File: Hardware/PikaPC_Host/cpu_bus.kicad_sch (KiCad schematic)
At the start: 33 parts, among them SW1 SW_Push, U1 PPC403GA, U3 MCP120-315GI/TO, Y1 25M

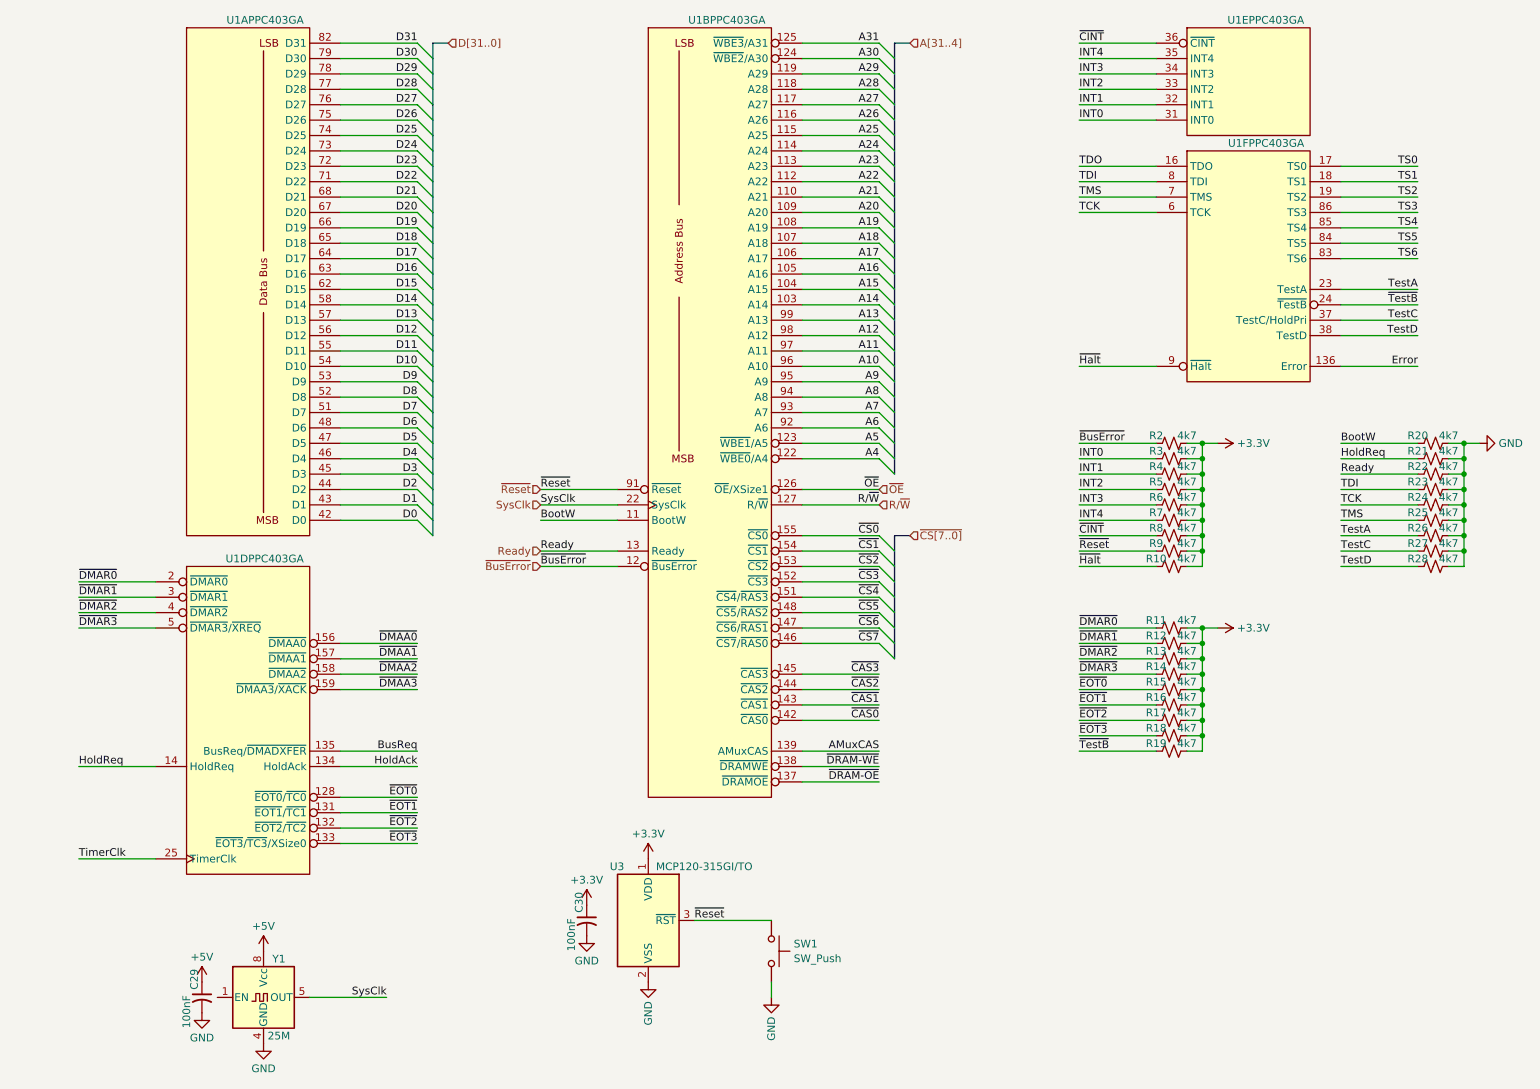
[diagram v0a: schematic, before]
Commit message: Rework bus pinout
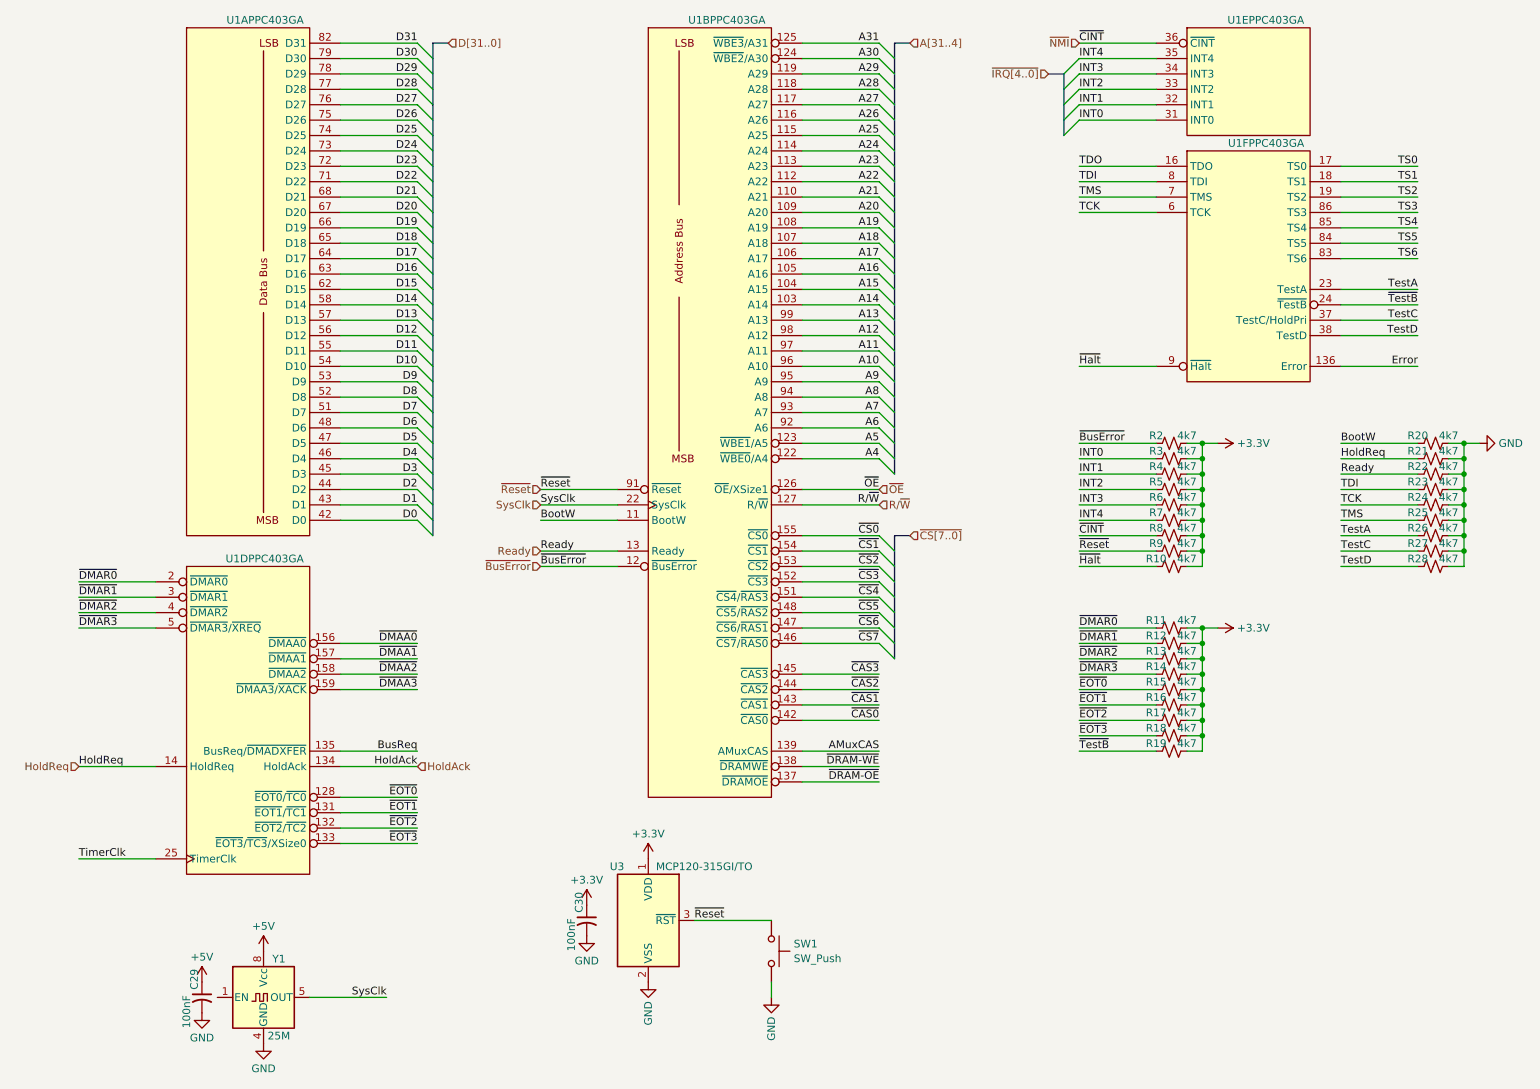
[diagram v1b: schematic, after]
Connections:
- net ~{CINT} renamed ~{NMI}
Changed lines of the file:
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@@
 	)
 	(bus_entry
+		(at 185.42 40.64)
+		(size -2.54 2.54)
+		(stroke
+			(width 0)
+			(type default)
+		)
+	)
+	(bus_entry
 		(at 152.4 119.38)
 		(size 2.54 2.54)
@@
 	)
 	(bus_entry
+		(at 185.42 38.1)
+		(size -2.54 2.54)
+		(stroke
+			(width 0)
+			(type default)
+		)
+	)
+	(bus_entry
 		(at 152.4 35.56)
 		(size 2.54 2.54)
@@
 	)
 	(bus_entry
+		(at 185.42 35.56)
+		(size -2.54 2.54)
+		(stroke
+			(width 0)
+			(type default)
+		)
+	)
+	(bus_entry
+		(at 185.42 33.02)
+		(size -2.54 2.54)
+		(stroke
+			(width 0)
+			(type default)
+		)
+	)
+	(bus_entry
 		(at 76.2 106.68)
 		(size 2.54 2.54)
@@
 	)
 	(bus_entry
+		(at 185.42 30.48)
+		(size -2.54 2.54)
+		(stroke
+			(width 0)
+			(type default)
+		)
+	)
+	(bus_entry
 		(at 152.4 30.48)
 		(size 2.54 2.54)
@@
 	(bus
 		(pts
+			(xy 180.34 33.02) (xy 182.88 33.02)
+		)
+		(stroke
+			(width 0)
+			(type default)
+		)
+	)
+	(bus
+		(pts
 			(xy 78.74 50.8) (xy 78.74 48.26)
 		)
@@
 		)
 	)
+	(bus
+		(pts
+			(xy 182.88 33.02) (xy 182.88 35.56)
+		)
+		(stroke
+			(width 0)
+			(type default)
+		)
+	)
 	(wire
 		(pts
@@
 		)
 	)
+	(bus
+		(pts
+			(xy 182.88 35.56) (xy 182.88 38.1)
+		)
+		(stroke
+			(width 0)
+			(type default)
+		)
+	)
 	(wire
 		(pts
@@
 		)
 	)
+	(bus
+		(pts
+			(xy 182.88 38.1) (xy 182.88 40.64)
+		)
+		(stroke
+			(width 0)
+			(type default)
+		)
+	)
 	(wire
 		(pts
@@
 		)
 	)
+	(bus
+		(pts
+			(xy 182.88 40.64) (xy 182.88 43.18)
+		)
+		(stroke
+			(width 0)
+			(type default)
+		)
+	)
 	(wire
 		(pts
@@
 		)
 	)
+	(hierarchical_label "HoldReq"
+		(shape input)
+		(at 20.32 147.32 180)
+		(effects
+			(font
+				(size 1.27 1.27)
+			)
+			(justify right)
+		)
+	)
 	(hierarchical_label "Ready"
 		(shape input)
@@
 		)
 	)
+	(hierarchical_label "~{NMI}"
+		(shape input)
+		(at 185.42 27.94 180)
+		(effects
+			(font
+				(size 1.27 1.27)
+			)
+			(justify right)
+		)
+	)
 	(hierarchical_label "~{BusError}"
 		(shape input)
@@
 		)
 	)
+	(hierarchical_label "~{IRQ[4..0]}"
+		(shape input)
+		(at 180.34 33.02 180)
+		(effects
+			(font
+				(size 1.27 1.27)
+			)
+			(justify right)
+		)
+	)
 	(hierarchical_label "D[31..0]"
 		(shape input)
@@
 		)
 	)
+	(hierarchical_label "HoldAck"
+		(shape input)
+		(at 76.2 147.32 0)
+		(effects
+			(font
+				(size 1.27 1.27)
+			)
+			(justify left)
+		)
+	)

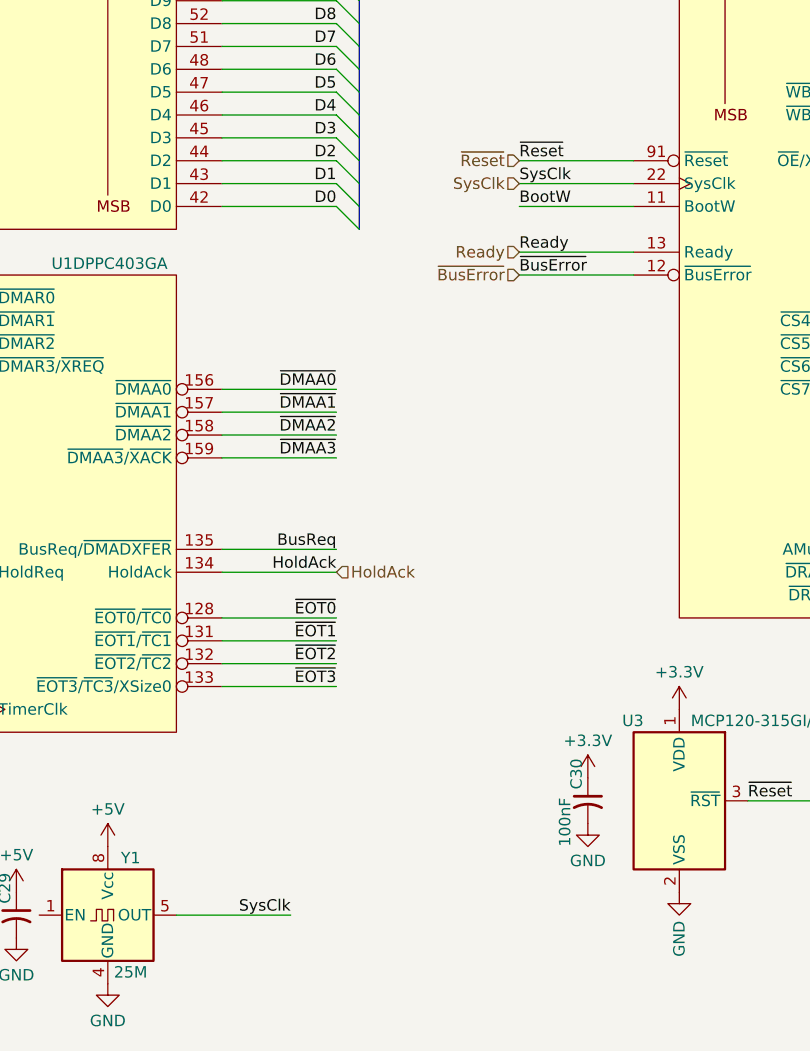
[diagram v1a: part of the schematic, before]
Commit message: Host Card refinement
add main bus clock selection
silkscreen cleanup
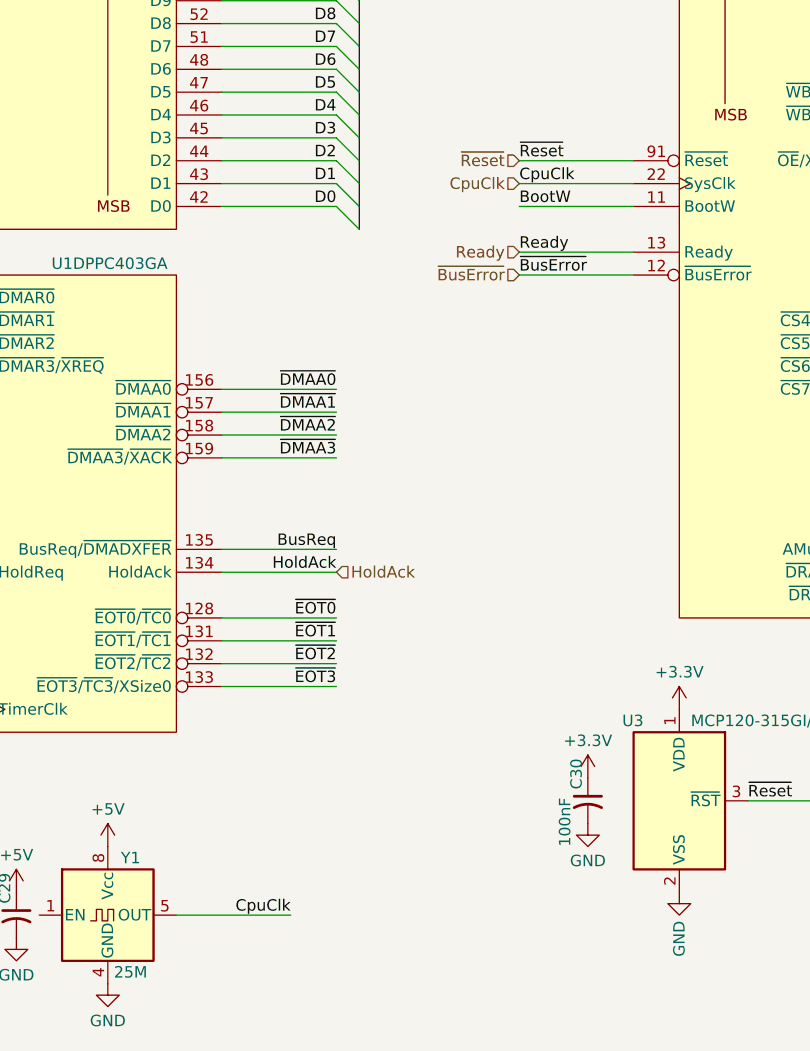
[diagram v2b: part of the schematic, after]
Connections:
- net SysClk renamed CpuClk
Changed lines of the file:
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@@
 		)
 	)
-	(label "SysClk"
+	(label "CpuClk"
 		(at 71.12 185.42 180)
 		(effects
@@
 		)
 	)
-	(label "SysClk"
+	(label "CpuClk"
 		(at 96.52 104.14 0)
 		(effects
@@
 		)
 	)
-	(hierarchical_label "SysClk"
+	(hierarchical_label "CpuClk"
 		(shape input)
 		(at 96.52 104.14 180)

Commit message: Annotate & prep for output - Host & KBC
add gerber output to gitignore
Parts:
- C29, C30: Mouser (none) -> 187-CL21B104KACNNNC
- R10, R11, R12, R13, R14, R15, R16, R17, R18, R19, R2, R20, R21, R22, R23, R24, R25, R26, R27, R28, R3, R4, R5, R6, R7, R8, R9: Mouser (none) -> 303-0805W8J0472T5E
- U3: Mouser (none) -> 579-MCP120-315GI/TO

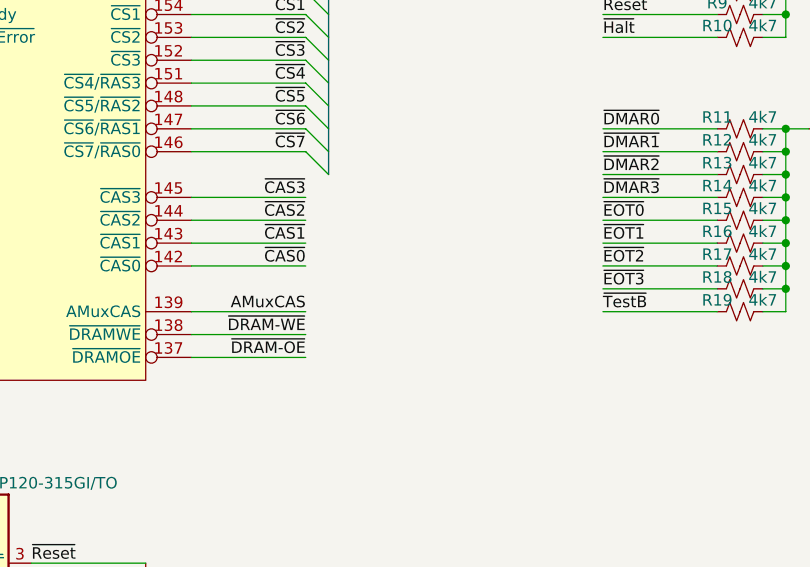
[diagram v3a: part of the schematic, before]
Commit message: Host Card updates
- add missing bus pull-ups
- add on-board DRAM
- add series termination resistors to AD bus
- fix DE9 footprint mounting hole location
- fix double-buffered bus clock
- use 74'2244 buffer w/series term resistors for bus control signals
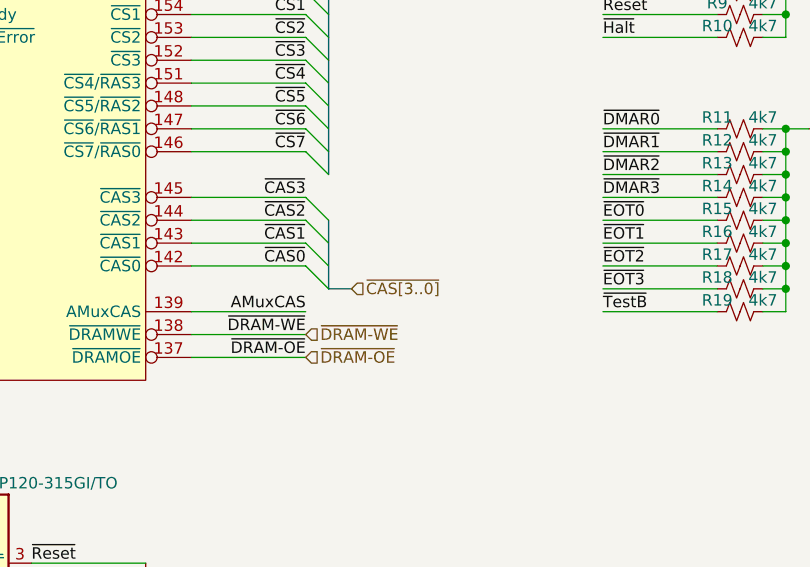
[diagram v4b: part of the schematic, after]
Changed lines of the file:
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@@
 	)
 	(bus_entry
+		(at 152.4 139.7)
+		(size 2.54 2.54)
+		(stroke
+			(width 0)
+			(type default)
+		)
+	)
+	(bus_entry
 		(at 152.4 45.72)
 		(size 2.54 2.54)
@@
 	)
 	(bus_entry
+		(at 152.4 134.62)
+		(size 2.54 2.54)
+		(stroke
+			(width 0)
+			(type default)
+		)
+	)
+	(bus_entry
 		(at 76.2 33.02)
 		(size 2.54 2.54)
@@
 	)
 	(bus_entry
+		(at 152.4 132.08)
+		(size 2.54 2.54)
+		(stroke
+			(width 0)
+			(type default)
+		)
+	)
+	(bus_entry
 		(at 76.2 55.88)
 		(size 2.54 2.54)
@@
 	)
 	(bus_entry
+		(at 152.4 137.16)
+		(size 2.54 2.54)
+		(stroke
+			(width 0)
+			(type default)
+		)
+	)
+	(bus_entry
 		(at 152.4 127)
 		(size 2.54 2.54)
@@
 		)
 	)
+	(bus
+		(pts
+			(xy 154.94 142.24) (xy 157.48 142.24)
+		)
+		(stroke
+			(width 0)
+			(type default)
+		)
+	)
 	(wire
 		(pts
@@
 	(bus
 		(pts
+			(xy 154.94 139.7) (xy 154.94 142.24)
+		)
+		(stroke
+			(width 0)
+			(type default)
+		)
+	)
+	(bus
+		(pts
 			(xy 154.94 91.44) (xy 154.94 88.9)
 		)
@@
 		)
 	)
+	(bus
+		(pts
+			(xy 154.94 137.16) (xy 154.94 139.7)
+		)
+		(stroke
+			(width 0)
+			(type default)
+		)
+	)
+	(bus
+		(pts
+			(xy 154.94 134.62) (xy 154.94 137.16)
+		)
+		(stroke
+			(width 0)
+			(type default)
+		)
+	)
 	(wire
 		(pts
@@
 		)
 	)
+	(hierarchical_label "~{DRAM-OE}"
+		(shape input)
+		(at 152.4 149.86 0)
+		(effects
+			(font
+				(size 1.27 1.27)
+			)
+			(justify left)
+		)
+	)
 	(hierarchical_label "~{BusError}"
 		(shape input)
@@
 		)
 	)
+	(hierarchical_label "~{CAS[3..0]}"
+		(shape input)
+		(at 157.48 142.24 0)
+		(effects
+			(font
+				(size 1.27 1.27)
+			)
+			(justify left)
+		)
+	)
 	(hierarchical_label "~{CS[7..0]}"
 		(shape input)
@@
 		(effects
 			(font
+				(size 1.27 1.27)
+			)
+			(justify left)
+		)
+	)
+	(hierarchical_label "~{DRAM-WE}"
+		(shape input)
+		(at 152.4 147.32 0)
+		(effects
+			(font
